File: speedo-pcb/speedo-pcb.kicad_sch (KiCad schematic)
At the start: 57 parts, among them J1 Debug, J2 Mode, J3 Speedo, J4 Power, J5 VBAT, J6 BOOT, J7 Breakout, M1 X27_128, U1 XC6206P332MR, U3 OLED_128x32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

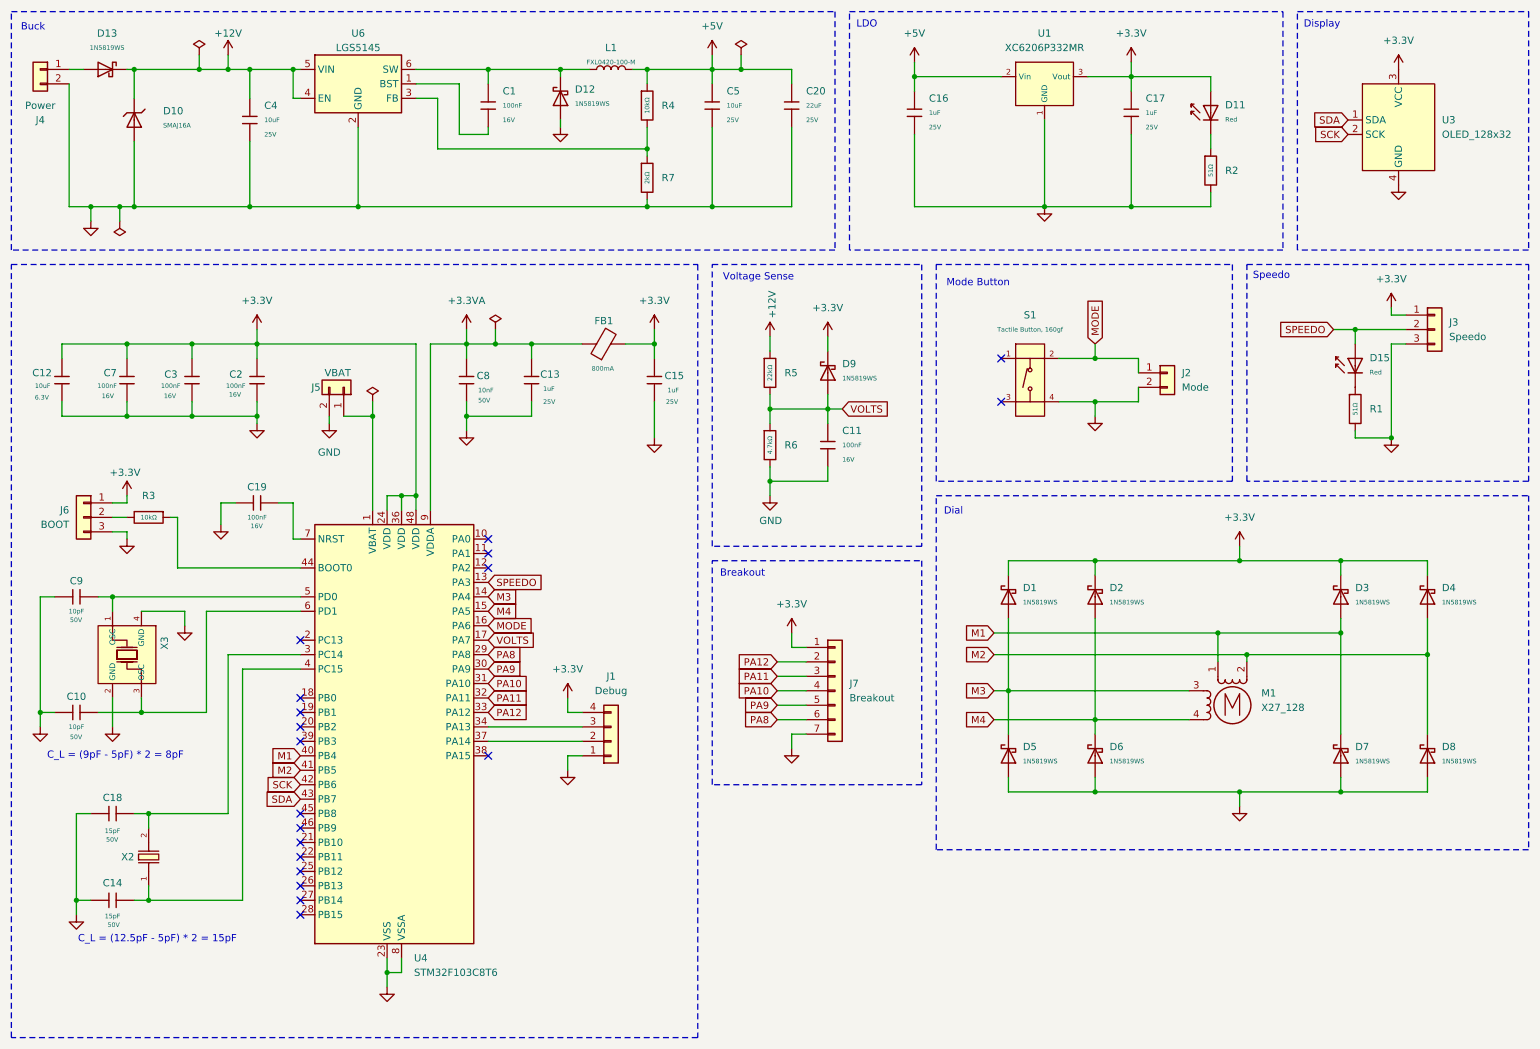
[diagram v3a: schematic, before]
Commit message: oled decoupling capacitor and i2c pull up resistors
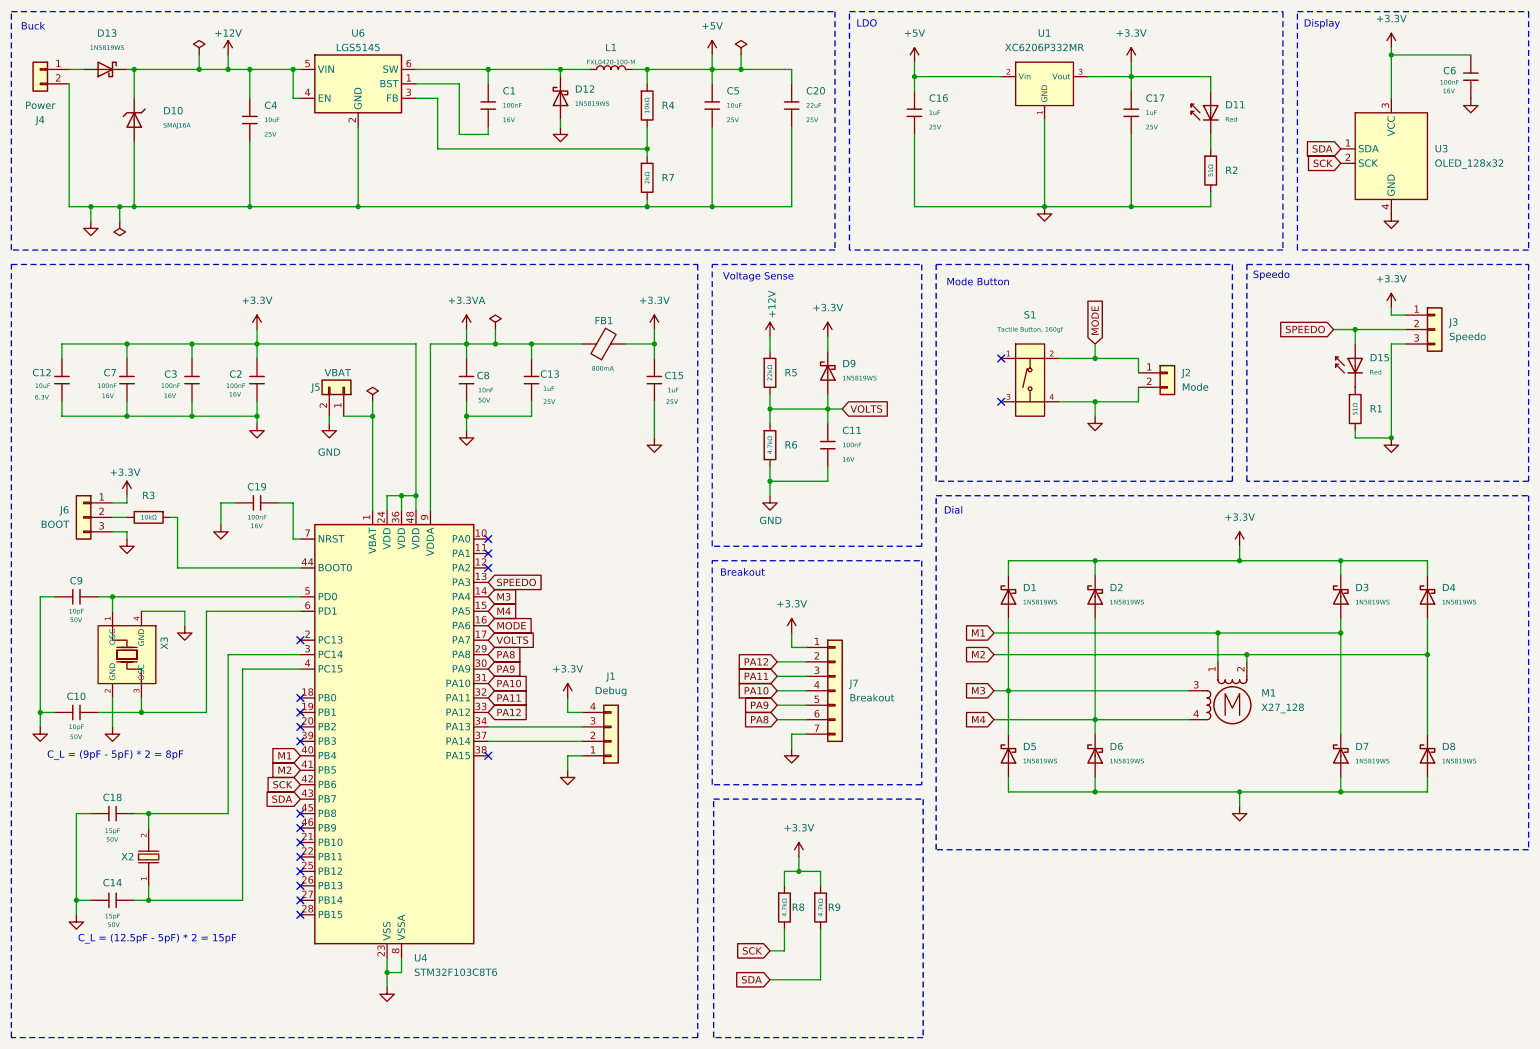
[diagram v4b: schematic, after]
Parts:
- added C6: 100nF, PCM_JLCPCB:C_0402, symbol PCM_JLCPCB-Capacitors:0402,100nF
- added R8, R9: 4.7kΩ, PCM_JLCPCB:R_0402, symbol PCM_JLCPCB-Resistors:0402,4.7kΩ
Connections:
- net +3.3V: now also C6.1, R8.1, R9.1
- net GND: now also C6.2
- net SCK: now also R8.2
- net SDA: now also R9.2
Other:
- moved on the sheet: U3

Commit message: u6 lcsc
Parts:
- U6: LCSC (none) -> C5123971
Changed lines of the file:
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@@
+			)
+		)
+		(property "LCSC" "C5123971"
+			(at 76.2 27.94 0)
+			(effects
+				(font
+					(size 1.27 1.27)
+				)
+				(hide yes)
 			)
 		)
